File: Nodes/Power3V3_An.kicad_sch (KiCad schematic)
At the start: 7 parts, among them IC6 TPS22995HQDDCRQ1, T23 Conn_01x01, T8 Conn_01x01

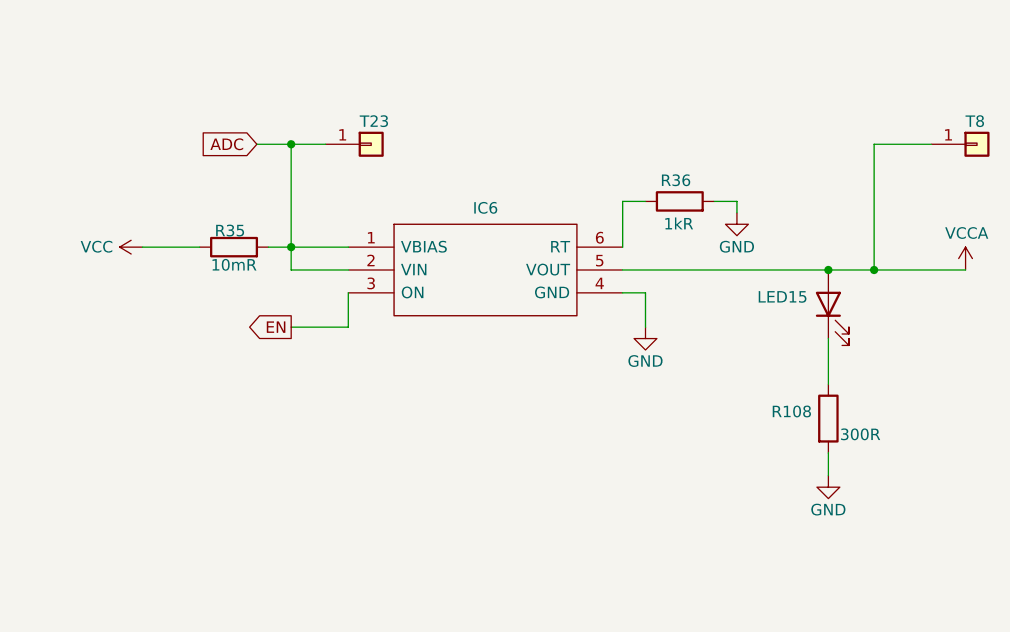
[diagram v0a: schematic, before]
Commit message: Nodes v2.2
- This version not compatible with BOB v.2.1.2 and older!
- Completely new layout design
- New power supply system with new voltage regulators
- New microchip STM32G431RBTx for the Analog Node
- New connection system (instead of 18 pin headers now 8 pin and pins were grouped by functions)
- Reduced size of the board by 5%
- Removed power switch for the Analog Node (because this functionality is now provided by a separate voltage regulator. for a more stable voltage)
- Removable ground from the holes added
- Layer numbers added
- Small improvements of the components information were made
- New oscillator for the Nodes
- Removed CAN1, so now only one CAN connection due to the capabilities of the new microchip
- Other small changes and fixes on the schematic and design
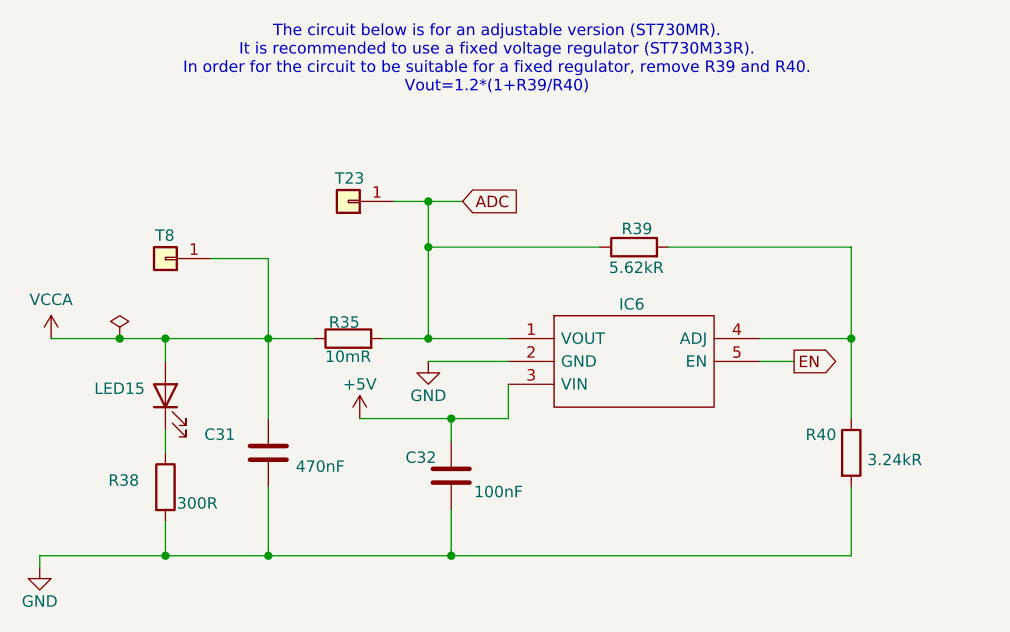
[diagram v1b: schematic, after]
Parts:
- removed IC6: TPS22995HQDDCRQ1, Button_Switch_SMD:SOT95P280X110-6N, symbol Power_Switch:TPS22995HQDDCRQ1
- removed R108: 300R, Resistor_SMD:R_0805_2012Metric_Pad1.20x1.40mm_HandSolder, symbol Device:R
- removed R36: 1kR, Resistor_SMD:R_0805_2012Metric_Pad1.20x1.40mm_HandSolder, symbol Device:R
- added C31: 470nF, Capacitor_SMD:C_0805_2012Metric_Pad1.18x1.45mm_HandSolder, symbol Device:C
- added C32: 100nF, Capacitor_SMD:C_0805_2012Metric_Pad1.18x1.45mm_HandSolder, symbol Device:C
- added IC6: ST730MR, Regulators:SOT95P280X145-5N, symbol Regulator_Linear:ST730MR
- added R38: 300R, Resistor_SMD:R_0805_2012Metric_Pad1.20x1.40mm_HandSolder, symbol Device:R
- added R39: 5.62kR, Resistor_SMD:R_0805_2012Metric_Pad1.20x1.40mm_HandSolder, symbol Device:R
- added R40: 3.24kR, Resistor_SMD:R_0805_2012Metric_Pad1.20x1.40mm_HandSolder, symbol Device:R
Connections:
- net VCC is gone; now on net VCCA: R35.1
- net ADC: now also IC6.1 (VOUT), R39.1
- net EN: now also IC6.5 (EN)
- net GND: now also C31.2, C32.2, IC6.2 (GND), R38.2, R40.2
- net VCCA: now also C31.1
- net at LED15.1 (K): now also R38.1
- new net: IC6.4 (ADJ), R39.2, R40.1
- new net +5V: C32.1, IC6.3 (VIN)
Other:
- note added: "The circuit below is for an adjustable version (ST730MR). It is recommended to use a fixed voltage regulator (ST730M33R). In order for the circuit to be suitable for a fixed regulator, remove R39 and R40. Vout=1.2*(1+R39/R40)"

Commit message: Nodes v2.2.3
- Added one more PWM Level shifter
- Controllable amplitude of PWM by switches
- Added labels
- Added resistors to solve BOOT issue
- I2C1 pins changed
- More GND vias
- Higher resistance for adjustable voltage regulators
- Other small changes
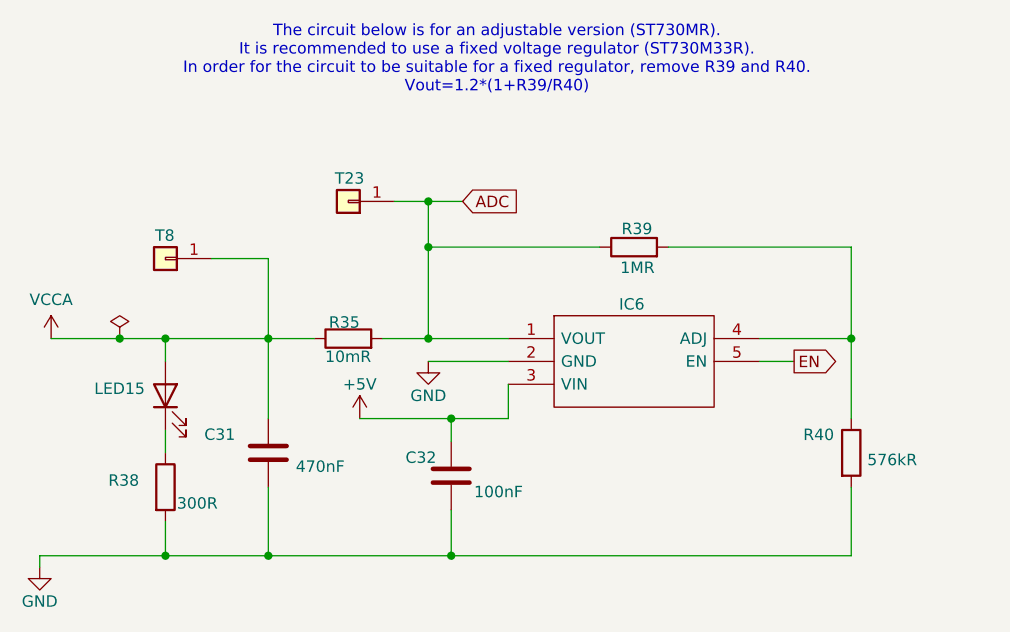
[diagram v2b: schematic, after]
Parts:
- R39: value 5.62kR -> 1MR
- R40: value 3.24kR -> 576kR
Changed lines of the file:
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@@
 		(dnp no)
 		(property "Reference" "R40"
-			(at 176.53 101.6 0)
-			(effects
-				(font
-					(size 1.27 1.27)
-				)
-				(justify left bottom)
-			)
-		)
-		(property "Value" "3.24kR"
+			(at 176.276 101.6 0)
+			(effects
+				(font
+					(size 1.27 1.27)
+				)
+				(justify left bottom)
+			)
+		)
+		(property "Value" "576kR"
 			(at 183.388 104.394 0)
 			(effects
@@
 			)
 		)
-		(property "Description" "ERJ-PB6B3241V"
+		(property "Description" "ERJ-6ENF5763V"
 			(at 181.61 102.87 0)
 			(effects
@@
 			)
 		)
-		(property "Value" "5.62kR"
-			(at 160.782 82.296 90)
+		(property "Value" "1MR"
+			(at 159.766 82.296 90)
 			(effects
 				(font
@@
 			)
 		)
-		(property "Datasheet" "https://www.mouser.fi/datasheet/2/54/cr-1858361.pdf"
+		(property "Datasheet" ""
 			(at 157.48 80.01 0)
 			(effects
@@
 			)
 		)
-		(property "Description" "CR0805-FX-5621ELF"
+		(property "Description" "TNPW08051M00BEEN"
 			(at 157.48 80.01 0)
 			(effects
